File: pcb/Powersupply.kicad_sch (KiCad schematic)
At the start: 39 parts, among them J1 Conn_02x04_Odd_Even, U5 TPS54325PWP.d, U6 TPS54294PWP

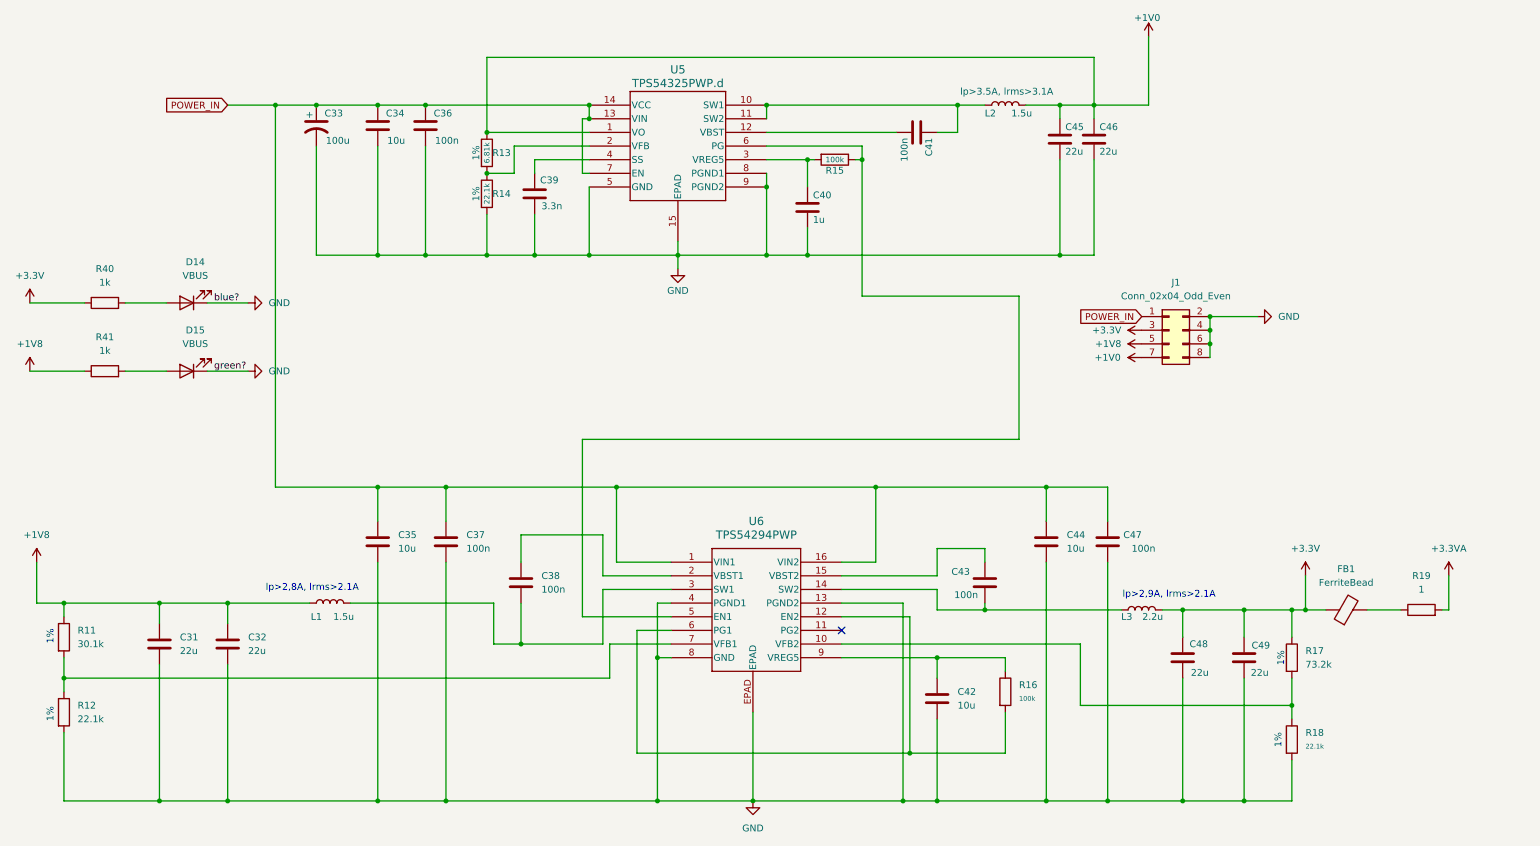
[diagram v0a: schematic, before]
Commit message: fixed erc errors
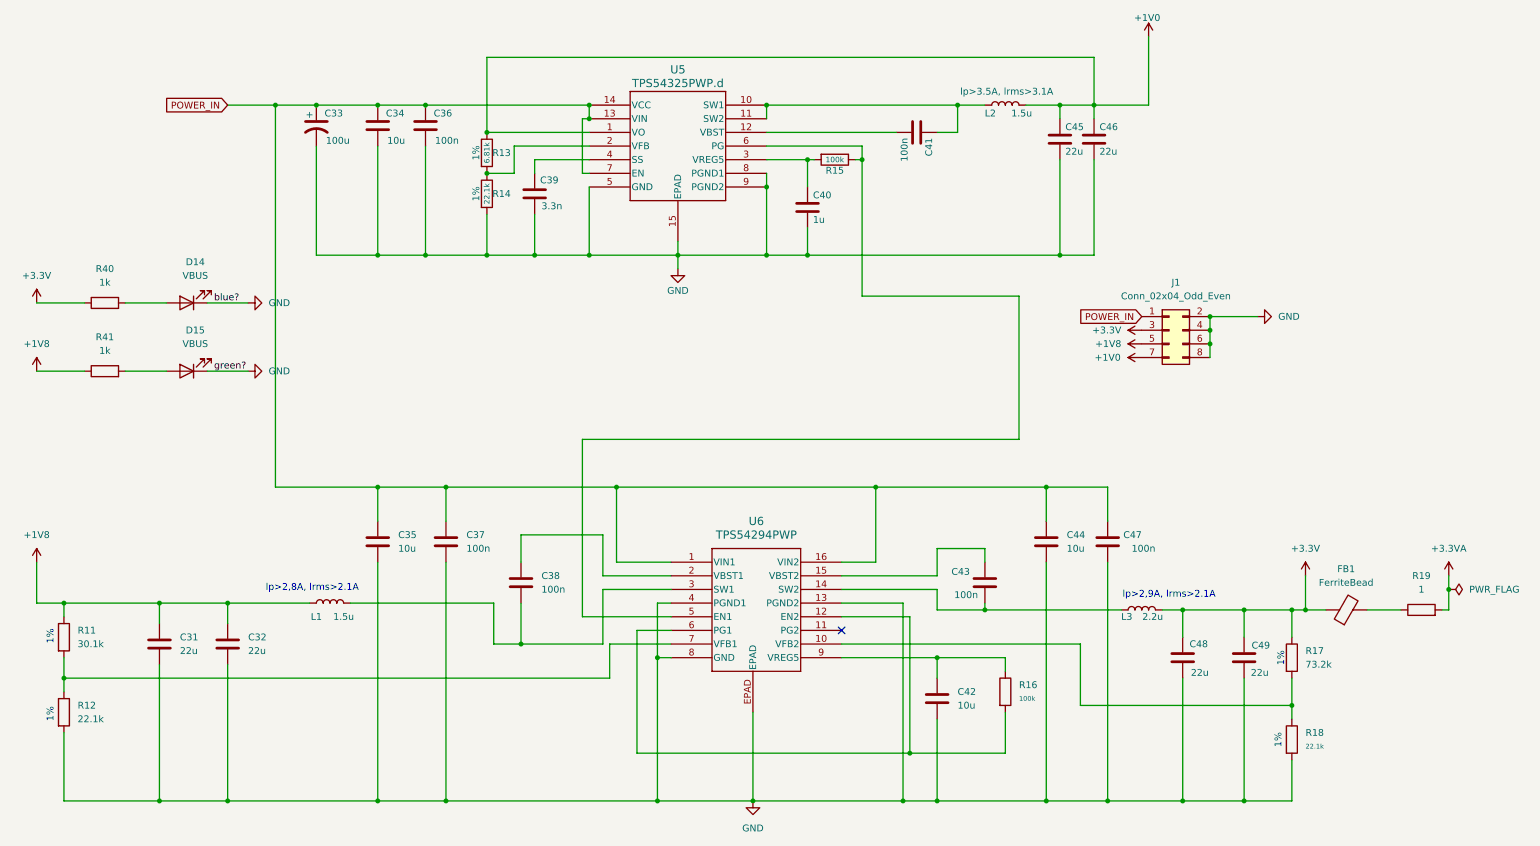
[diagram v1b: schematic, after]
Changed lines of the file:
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@@
 	)
 	(junction
+		(at 278.13 123.19)
+		(diameter 0)
+		(color 0 0 0 0)
+	)
+	(junction
 		(at 151.13 33.02)
 		(diameter 0)
@@
 	(wire
 		(pts
-			(xy 278.13 120.65) (xy 278.13 127)
+			(xy 278.13 120.65) (xy 278.13 123.19)
 		)
 		(stroke
@@
 	(wire
 		(pts
-			(xy 24.13 69.85) (xy 13.97 69.85)
+			(xy 24.13 69.85) (xy 15.24 69.85)
 		)
 		(stroke
@@
 	(wire
 		(pts
+			(xy 278.13 123.19) (xy 278.13 127)
+		)
+		(stroke
+			(width 0)
+			(type default)
+		)
+	)
+	(wire
+		(pts
 			(xy 20.32 125.73) (xy 20.32 128.27)
 		)
@@
 	(wire
 		(pts
-			(xy 24.13 82.55) (xy 13.97 82.55)
+			(xy 24.13 82.55) (xy 15.24 82.55)
 		)
 		(stroke
@@
 	(symbol
 		(lib_id "power:+3.3V")
-		(at 13.97 69.85 0)
+		(at 15.24 69.85 0)
 		(unit 1)
 		(body_style 1)
@@
 		(fields_autoplaced yes)
 		(property "Reference" "#PWR057"
-			(at 13.97 73.66 0)
+			(at 15.24 73.66 0)
 			(hide yes)
 			(show_name no)
@@
 		)
 		(property "Value" "+3.3V"
-			(at 13.97 64.77 0)
+			(at 15.24 64.77 0)
 			(show_name no)
 			(do_not_autoplace no)
@@
 		)
 		(property "Footprint" ""
-			(at 13.97 69.85 0)
+			(at 15.24 69.85 0)
 			(hide yes)
 			(show_name no)
@@
 		)
 		(property "Datasheet" ""
-			(at 13.97 69.85 0)
+			(at 15.24 69.85 0)
 			(hide yes)
 			(show_name no)
@@
 		)
 		(property "Description" "Power symbol creates a global label with name \"+3.3V\""
-			(at 13.97 69.85 0)
+			(at 15.24 69.85 0)
 			(hide yes)
 			(show_name no)
@@
 	(symbol
 		(lib_id "power:+1V8")
-		(at 13.97 82.55 0)
+		(at 15.24 82.55 0)
 		(unit 1)
 		(body_style 1)
@@
 		(fields_autoplaced yes)
 		(property "Reference" "#PWR079"
-			(at 13.97 86.36 0)
+			(at 15.24 86.36 0)
 			(hide yes)
 			(show_name no)
@@
 		)
 		(property "Value" "+1V8"
-			(at 13.97 77.47 0)
+			(at 15.24 77.47 0)
 			(show_name no)
 			(do_not_autoplace no)
@@
 		)
 		(property "Footprint" ""
-			(at 13.97 82.55 0)
+			(at 15.24 82.55 0)
 			(hide yes)
 			(show_name no)
@@
 		)
 		(property "Datasheet" ""
-			(at 13.97 82.55 0)
+			(at 15.24 82.55 0)
 			(hide yes)
 			(show_name no)
@@
 		)
 		(property "Description" "Power symbol creates a global label with name \"+1V8\""
-			(at 13.97 82.55 0)
+			(at 15.24 82.55 0)
 			(hide yes)
 			(show_name no)
@@
 					(unit 1)
 				)
+			)
+		)
+	)
+	(symbol
+		(lib_id "power:PWR_FLAG")
+		(at 278.13 123.19 270)
+		(unit 1)
+		(body_style 1)
+		(exclude_from_sim no)
+		(in_bom yes)
+		(on_board yes)
+		(in_pos_files yes)
+		(dnp no)
+		(fields_autoplaced yes)
+		(property "Reference" "#FLG01"
+			(at 280.035 123.19 0)
+			(hide yes)
+			(show_name no)
+			(do_not_autoplace no)
+			(effects
+				(font
+					(size 1.27 1.27)
+				)
+			)
+		)
+		(property "Value" "PWR_FLAG"
+			(at 281.94 123.1899 90)
+			(show_name no)
+			(do_not_autoplace no)
+			(effects
+				(font
+					(size 1.27 1.27)
+				)
+				(justify left)
+			)
+		)
+		(property "Footprint" "Package_SO:TSSOP-28_4.4x9.7mm_P0.65mm"
+			(at 278.13 123.19 0)
+			(hide yes)
+			(show_name no)
+			(do_not_autoplace no)
+			(effects
+				(font
+					(size 1.27 1.27)
+				)
+			)
+		)
+		(property "Datasheet" ""
+			(at 278.13 123.19 0)
+			(hide yes)
+			(show_name no)
+			(do_not_autoplace no)
+			(effects
+				(font
+					(size 1.27 1.27)
+				)
+			)
+		)
+		(property "Description" "Special symbol for telling ERC where power comes from"
+			(at 278.13 123.19 0)
+			(hide yes)
+			(show_name no)
+			(do_not_autoplace no)
+			(effects
+				(font
+					(size 1.27 1.27)
+				)
+			)
+		)
+		(pin "1"
+		)
+		(instances
+			(project "tdt4295"
+				(path "/603dd496-f9c4-4a31-9104-19eec41ebc98/634870db-7705-458e-b29f-8b3e7772e7aa"
+					(reference "#FLG01")
+					(unit 1)
+				)

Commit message: pcb: fix erc
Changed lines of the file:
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@@
 	)
 	(junction
+		(at 251.46 124.4903)
+		(diameter 0)
+		(color 0 0 0 0)
+	)
+	(junction
 		(at 38.1 162.56)
 		(diameter 0)
@@
 	(wire
 		(pts
-			(xy 251.46 120.65) (xy 251.46 127)
+			(xy 251.46 120.65) (xy 251.46 124.4903)
 		)
 		(stroke
@@
 	(wire
 		(pts
+			(xy 251.46 124.4903) (xy 251.46 127)
+		)
+		(stroke
+			(width 0)
+			(type default)
+		)
+	)
+	(wire
+		(pts
 			(xy 177.8 153.67) (xy 195.58 153.67)
 		)
@@
 					(unit 1)
 				)
+			)
+		)
+	)
+	(symbol
+		(lib_id "power:PWR_FLAG")
+		(at 251.46 124.4903 90)
+		(unit 1)
+		(body_style 1)
+		(exclude_from_sim no)
+		(in_bom yes)
+		(on_board yes)
+		(in_pos_files yes)
+		(dnp no)
+		(fields_autoplaced yes)
+		(property "Reference" "#FLG06"
+			(at 249.555 124.4903 0)
+			(hide yes)
+			(show_name no)
+			(do_not_autoplace no)
+			(effects
+				(font
+					(size 1.27 1.27)
+				)
+			)
+		)
+		(property "Value" "PWR_FLAG"
+			(at 247.65 124.4902 90)
+			(show_name no)
+			(do_not_autoplace no)
+			(effects
+				(font
+					(size 1.27 1.27)
+				)
+				(justify left)
+			)
+		)
+		(property "Footprint" "Package_SO:TSSOP-28_4.4x9.7mm_P0.65mm"
+			(at 251.46 124.4903 0)
+			(hide yes)
+			(show_name no)
+			(do_not_autoplace no)
+			(effects
+				(font
+					(size 1.27 1.27)
+				)
+			)
+		)
+		(property "Datasheet" ""
+			(at 251.46 124.4903 0)
+			(hide yes)
+			(show_name no)
+			(do_not_autoplace no)
+			(effects
+				(font
+					(size 1.27 1.27)
+				)
+			)
+		)
+		(property "Description" "Special symbol for telling ERC where power comes from"
+			(at 251.46 124.4903 0)
+			(hide yes)
+			(show_name no)
+			(do_not_autoplace no)
+			(effects
+				(font
+					(size 1.27 1.27)
+				)
+			)
+		)
+		(pin "1"
+		)
+		(instances
+			(project "tdt4295"
+				(path "/603dd496-f9c4-4a31-9104-19eec41ebc98/634870db-7705-458e-b29f-8b3e7772e7aa"
+					(reference "#FLG06")
+					(unit 1)
+				)

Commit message: pcb: satisfy ERC warnings and errors
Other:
- note added: "blue?"
- note added: "green?"
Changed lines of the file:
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@@
 	(generator_version "10.0")
 	(paper "A4")
+	(text "blue?"
+		(exclude_from_sim no)
+		(at 48.26 69.85 0)
+		(effects
+			(font
+				(size 1.27 1.27)
+			)
+			(justify left bottom)
+		)
+	)
 	(text "lp>2,9A, lrms>2.1A"
 		(exclude_from_sim no)
@@
 		)
 	)
+	(text "green?"
+		(exclude_from_sim no)
+		(at 48.26 82.55 0)
+		(effects
+			(font
+				(size 1.27 1.27)
+			)
+			(justify left bottom)
+		)
+	)
 	(text "1%\n"
 		(exclude_from_sim no)
@@
 	)
 	(junction
-		(at 251.46 124.4903)
-		(diameter 0)
-		(color 0 0 0 0)
-	)
-	(junction
 		(at 38.1 162.56)
 		(diameter 0)
@@
 	)
 	(junction
+		(at 251.46 127)
+		(diameter 0)
+		(color 0 0 0 0)
+	)
+	(junction
 		(at 107.95 60.96)
 		(diameter 0)
@@
 	)
 	(junction
-		(at 251.46 127)
-		(diameter 0)
-		(color 0 0 0 0)
-	)
-	(junction
 		(at 78.74 104.14)
 		(diameter 0)
@@
 	)
 	(junction
+		(at 251.46 123.19)
+		(diameter 0)
+		(color 0 0 0 0)
+	)
+	(junction
 		(at 67.31 33.02)
 		(diameter 0)
@@
 	(wire
 		(pts
-			(xy 251.46 120.65) (xy 251.46 124.4903)
-		)
-		(stroke
-			(width 0)
-			(type default)
-		)
-	)
-	(wire
-		(pts
 			(xy 107.95 53.34) (xy 107.95 60.96)
 		)
@@
 	(wire
 		(pts
-			(xy 251.46 124.4903) (xy 251.46 127)
+			(xy 251.46 120.65) (xy 251.46 123.19)
 		)
 		(stroke
@@
 	(wire
 		(pts
+			(xy 251.46 123.19) (xy 251.46 127)
+		)
+		(stroke
+			(width 0)
+			(type default)
+		)
+	)
+	(wire
+		(pts
 			(xy 121.92 139.7) (xy 20.32 139.7)
 		)
@@
 		)
 	)
-	(label "blue?"
-		(at 48.26 69.85 0)
-		(effects
-			(font
-				(size 1.27 1.27)
-			)
-			(justify left bottom)
-		)
-	)
-	(label "green?"
-		(at 48.26 82.55 0)
-		(effects
-			(font
-				(size 1.27 1.27)
-			)
-			(justify left bottom)
-		)
-	)
 	(global_label "POWER_IN"
 		(shape input)
@@
 	(symbol
 		(lib_id "power:PWR_FLAG")
-		(at 251.46 124.4903 90)
+		(at 251.46 123.19 90)
 		(unit 1)
 		(body_style 1)
@@
 		(fields_autoplaced yes)
 		(property "Reference" "#FLG06"
-			(at 249.555 124.4903 0)
+			(at 249.555 123.19 0)
 			(hide yes)
 			(show_name no)
@@
 		)
 		(property "Value" "PWR_FLAG"
-			(at 247.65 124.4902 90)
+			(at 247.65 123.1899 90)
 			(show_name no)
 			(do_not_autoplace no)
@@
 		)
 		(property "Footprint" "Package_SO:TSSOP-28_4.4x9.7mm_P0.65mm"
-			(at 251.46 124.4903 0)
+			(at 251.46 123.19 0)
 			(hide yes)
 			(show_name no)
@@
 		)
 		(property "Datasheet" ""
-			(at 251.46 124.4903 0)
+			(at 251.46 123.19 0)
 			(hide yes)
 			(show_name no)
@@
 		)
 		(property "Description" "Special symbol for telling ERC where power comes from"
-			(at 251.46 124.4903 0)
+			(at 251.46 123.19 0)
 			(hide yes)
 			(show_name no)

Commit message: layout prep
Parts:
- C31, C32, C33, C34, C35, C36, C37, C38, C39, C40, C41, C42, C43, C44, C45, C46, C47, C48, C49: footprint (none) -> Capacitor_SMD:C_0805_2012Metric_Pad1.18x1.45mm_HandSolder
- D14: value VBUS -> blue?; footprint (none) -> LED_SMD:LED_0805_2012Metric_Pad1.15x1.40mm_HandSolder
- D15: value VBUS -> green?; footprint (none) -> LED_SMD:LED_0805_2012Metric_Pad1.15x1.40mm_HandSolder
- FB1, L2: footprint (none) -> Inductor_SMD:L_0805_2012Metric_Pad1.05x1.20mm_HandSolder
- J1: footprint (none) -> Connector_JST:JST_PUD_B08B-PUDSS_2x04_P2.00mm_Vertical
- L1, L3: footprint Relay_THT:Relay_DPDT_Kemet_EC2_NU_DoubleCoil -> Inductor_SMD:L_0805_2012Metric_Pad1.05x1.20mm_HandSolder
- R11, R12, R13, R14, R15, R16, R17, R18, R19: footprint (none) -> Resistor_SMD:R_0805_2012Metric_Pad1.20x1.40mm_HandSolder
- R40, R41: footprint Resistor_THT:R_Array_SIP13 -> Resistor_SMD:R_0805_2012Metric_Pad1.20x1.40mm_HandSolder
- U5: footprint PWP14_2P31X2P46 -> TPS54325PWP.d:PWP14_2P31X2P46
- U6: footprint PWP16_2P31X2P46 -> TPS54294PWP:PWP16_2P31X2P46
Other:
- note removed: "blue?"
- note removed: "green?"
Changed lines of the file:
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@@
 	(generator_version "10.0")
 	(paper "A4")
-	(text "blue?"
-		(exclude_from_sim no)
-		(at 48.26 69.85 0)
-		(effects
-			(font
-				(size 1.27 1.27)
-			)
-			(justify left bottom)
-		)
-	)
 	(text "lp>2,9A, lrms>2.1A"
 		(exclude_from_sim no)
@@
 		)
 	)
-	(text "green?"
-		(exclude_from_sim no)
-		(at 48.26 82.55 0)
-		(effects
-			(font
-				(size 1.27 1.27)
-			)
-			(justify left bottom)
-		)
-	)
 	(text "1%\n"
 		(exclude_from_sim no)
@@
 			)
 		)
-		(property "Footprint" ""
+		(property "Footprint" "Capacitor_SMD:C_0805_2012Metric_Pad1.18x1.45mm_HandSolder"
 			(at 239.0648 139.7 0)
 			(hide yes)
@@
 			)
 		)
-		(property "Footprint" ""
+		(property "Footprint" "Inductor_SMD:L_0805_2012Metric_Pad1.05x1.20mm_HandSolder"
 			(at 195.58 33.02 0)
 			(hide yes)
@@
 			)
 		)
-		(property "Footprint" ""
+		(property "Footprint" "Resistor_SMD:R_0805_2012Metric_Pad1.20x1.40mm_HandSolder"
 			(at 163.83 41.402 90)
 			(hide yes)
@@
 			)
 		)
-		(property "Footprint" ""
+		(property "Footprint" "Capacitor_SMD:C_0805_2012Metric_Pad1.18x1.45mm_HandSolder"
 			(at 51.7652 137.16 0)
 			(hide yes)
@@
 			)
 		)
-		(property "Footprint" ""
+		(property "Footprint" "Resistor_SMD:R_0805_2012Metric_Pad1.20x1.40mm_HandSolder"
 			(at 247.142 151.13 90)
 			(hide yes)
@@
 			)
 		)
-		(property "Footprint" ""
+		(property "Footprint" "Capacitor_SMD:C_0805_2012Metric_Pad1.18x1.45mm_HandSolder"
 			(at 79.7052 118.11 0)
 			(hide yes)
@@
 			)
 		)
-		(property "Footprint" "Resistor_THT:R_Array_SIP13"
+		(property "Footprint" "Resistor_SMD:R_0805_2012Metric_Pad1.20x1.40mm_HandSolder"
 			(at 27.94 71.628 90)
 			(hide yes)
@@
 			)
 		)
-		(property "Footprint" ""
+		(property "Footprint" "Capacitor_SMD:C_0805_2012Metric_Pad1.18x1.45mm_HandSolder"
 			(at 79.7052 40.64 0)
 			(hide yes)
@@
 			)
 		)
-		(property "Footprint" ""
+		(property "Footprint" "Resistor_SMD:R_0805_2012Metric_Pad1.20x1.40mm_HandSolder"
 			(at 273.05 128.778 90)
 			(hide yes)
@@
 			)
 		)
-		(property "Footprint" ""
+		(property "Footprint" "Capacitor_SMD:C_0805_2012Metric_Pad1.18x1.45mm_HandSolder"
 			(at 190.8048 125.73 0)
 			(hide yes)
@@
 			)
 		)
-		(property "Footprint" ""
+		(property "Footprint" "Resistor_SMD:R_0805_2012Metric_Pad1.20x1.40mm_HandSolder"
 			(at 247.142 135.89 90)
 			(hide yes)
@@
 			)
 		)
-		(property "Footprint" ""
+		(property "Footprint" "Capacitor_SMD:C_0805_2012Metric_Pad1.18x1.45mm_HandSolder"
 			(at 206.7052 43.18 0)
 			(hide yes)
@@
 			)
 		)
-		(property "Footprint" ""
+		(property "Footprint" "Capacitor_SMD:C_0805_2012Metric_Pad1.18x1.45mm_HandSolder"
 			(at 202.2348 118.11 0)
 			(hide yes)
@@
 			)
 		)
-		(property "Footprint" ""
+		(property "Footprint" "Capacitor_SMD:C_0805_2012Metric_Pad1.18x1.45mm_HandSolder"
 			(at 106.3752 125.73 0)
 			(hide yes)
@@
 			)
 		)
-		(property "Footprint" ""
+		(property "Footprint" "Capacitor_SMD:C_0805_2012Metric_Pad1.18x1.45mm_HandSolder"
 			(at 159.7152 55.88 0)
 			(hide yes)
@@
 			)
 		)
-		(property "Value" "VBUS"
+		(property "Value" "blue?"
 			(at 44.7675 64.77 0)
 			(show_name no)
@@
 			)
 		)
-		(property "Footprint" ""
+		(property "Footprint" "LED_SMD:LED_0805_2012Metric_Pad1.15x1.40mm_HandSolder"
 			(at 43.18 69.85 0)
 			(hide yes)
@@
 			)
 		)
-		(property "Footprint" "PWP14_2P31X2P46"
+		(property "Footprint" "TPS54325PWP.d:PWP14_2P31X2P46"
 			(at 92.71 60.96 0)
 			(hide yes)
@@
 			)
 		)
-		(property "Footprint" ""
+		(property "Footprint" "Resistor_SMD:R_0805_2012Metric_Pad1.20x1.40mm_HandSolder"
 			(at 193.802 142.24 90)
 			(hide yes)
@@
 			)
 		)
-		(property "Footprint" ""
+		(property "Footprint" "Resistor_SMD:R_0805_2012Metric_Pad1.20x1.40mm_HandSolder"
 			(at 97.282 41.91 90)
 			(hide yes)
@@
 			)
 		)
-		(property "Footprint" "PWP16_2P31X2P46"
+		(property "Footprint" "TPS54294PWP:PWP16_2P31X2P46"
 			(at 122.174 150.114 0)
 			(hide yes)
@@
 			)
 		)
-		(property "Footprint" ""
+		(property "Footprint" "Resistor_SMD:R_0805_2012Metric_Pad1.20x1.40mm_HandSolder"
 			(at 18.542 132.08 90)
 			(hide yes)
@@
 			)
 		)
-		(property "Footprint" ""
+		(property "Footprint" "Capacitor_SMD:C_0805_2012Metric_Pad1.18x1.45mm_HandSolder"
 			(at 92.4052 118.11 0)
 			(hide yes)
@@
 			)
 		)
-		(property "Footprint" "Relay_THT:Relay_DPDT_Kemet_EC2_NU_DoubleCoil"
+		(property "Footprint" "Inductor_SMD:L_0805_2012Metric_Pad1.05x1.20mm_HandSolder"
 			(at 220.98 127 0)
 			(hide yes)
@@
 			)
 		)
-		(property "Footprint" ""
+		(property "Footprint" "Capacitor_SMD:C_0805_2012Metric_Pad1.18x1.45mm_HandSolder"
 			(at 213.6648 118.11 0)
 			(hide yes)
@@
 			)
 		)
-		(property "Footprint" ""
+		(property "Footprint" "Capacitor_SMD:C_0805_2012Metric_Pad1.18x1.45mm_HandSolder"
 			(at 175.26 39.0652 0)
 			(hide yes)
@@
 			)
 		)
-		(property "Footprint" ""
+		(property "Footprint" "Capacitor_SMD:C_0805_2012Metric_Pad1.18x1.45mm_HandSolder"
 			(at 181.9148 147.32 0)
 			(hide yes)
@@
 			)
 		)
-		(property "Footprint" "Relay_THT:Relay_DPDT_Kemet_EC2_NU_DoubleCoil"
+		(property "Footprint" "Inductor_SMD:L_0805_2012Metric_Pad1.05x1.20mm_HandSolder"
 			(at 69.85 125.73 0)
 			(hide yes)
@@
 			)
 		)
-		(property "Footprint" ""
+		(property "Footprint" "Capacitor_SMD:C_0805_2012Metric_Pad1.18x1.45mm_HandSolder"
 			(at 39.0652 137.16 0)
 			(hide yes)
@@
 			)
 		)
-		(property "Footprint" "Resistor_THT:R_Array_SIP13"
+		(property "Footprint" "Resistor_SMD:R_0805_2012Metric_Pad1.20x1.40mm_HandSolder"
 			(at 27.94 84.328 90)
 			(hide yes)
@@
 			)
 		)
-		(property "Footprint" ""
+		(property "Footprint" "Inductor_SMD:L_0805_2012Metric_Pad1.05x1.20mm_HandSolder"
 			(at 259.08 128.778 90)
 			(hide yes)
@@
 			)
 		)
-		(property "Footprint" ""
+		(property "Footprint" "Capacitor_SMD:C_0805_2012Metric_Pad1.18x1.45mm_HandSolder"
 			(at 67.31 36.83 0)
 			(hide yes)
@@
 			)
 		)
-		(property "Footprint" ""
+		(property "Footprint" "Capacitor_SMD:C_0805_2012Metric_Pad1.18x1.45mm_HandSolder"
 			(at 108.9152 53.34 0)
 			(hide yes)
@@
 			)
 		)
-		(property "Footprint" ""
+		(property "Footprint" "Capacitor_SMD:C_0805_2012Metric_Pad1.18x1.45mm_HandSolder"
 			(at 88.5952 40.64 0)
 			(hide yes)
@@
 			)
 		)
-		(property "Footprint" ""
+		(property "Footprint" "Resistor_SMD:R_0805_2012Metric_Pad1.20x1.40mm_HandSolder"
 			(at 97.282 49.53 90)
 			(hide yes)
@@
 			)
 		)
-		(property "Footprint" ""
+		(property "Footprint" "Capacitor_SMD:C_0805_2012Metric_Pad1.18x1.45mm_HandSolder"
 			(at 213.0552 43.18 0)
 			(hide yes)
@@
 			)
 		)
-		(property "Footprint" ""
+		(property "Footprint" "Connector_JST:JST_PUD_B08B-PUDSS_2x04_P2.00mm_Vertical"
 			(at 226.06 74.93 0)
 			(hide yes)
@@
 			)
 		)
-		(property "Footprint" ""
+		(property "Footprint" "Resistor_SMD:R_0805_2012Metric_Pad1.20x1.40mm_HandSolder"
 			(at 18.542 146.05 90)
 			(hide yes)
@@
 			)
 		)
-		(property "Footprint" ""
+		(property "Footprint" "Capacitor_SMD:C_0805_2012Metric_Pad1.18x1.45mm_HandSolder"
 			(at 227.6348 139.7 0)
 			(hide yes)
@@
 			)
 		)
-		(property "Value" "VBUS"
+		(property "Value" "green?"
 			(at 44.7675 77.47 0)
 			(show_name no)
@@
 			)
 		)
-		(property "Footprint" ""
+		(property "Footprint" "LED_SMD:LED_0805_2012Metric_Pad1.15x1.40mm_HandSolder"
 			(at 43.18 82.55 0)
 			(hide yes)

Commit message: updates labels
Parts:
- renumbered D14 to D1, D15 to D2, J1 to J2, R11 to R25, R12 to R26, R40 to R27, R41 to R28, R13 to R29, R14 to R30, R15 to R31, R16 to R32, R17 to R33, R18 to R34, R19 to R35
